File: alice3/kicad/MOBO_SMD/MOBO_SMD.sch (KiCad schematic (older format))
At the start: 0 parts

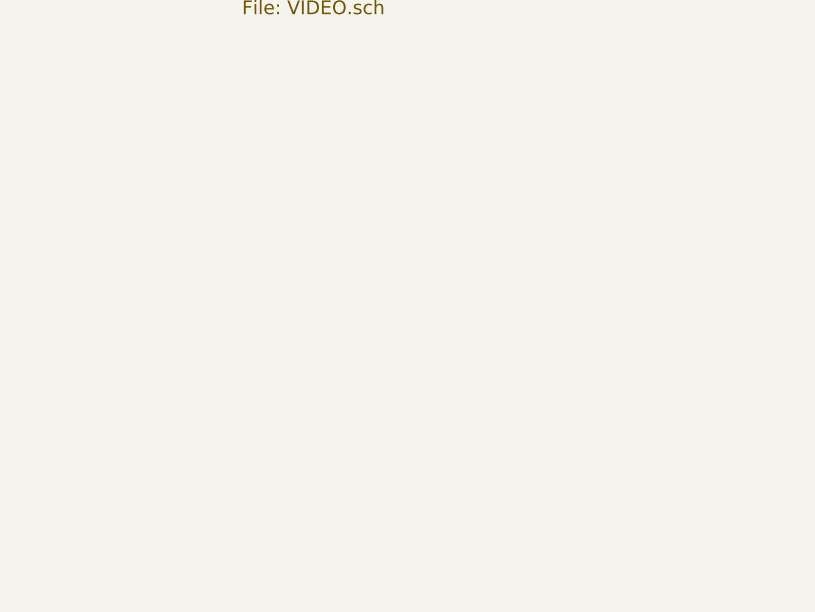
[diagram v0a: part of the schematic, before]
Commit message: Continuing to integrate STM32F415RG parts
Power circuit
STM32F415RG power and ground and BOOT pins
MicroSD card component and footprint
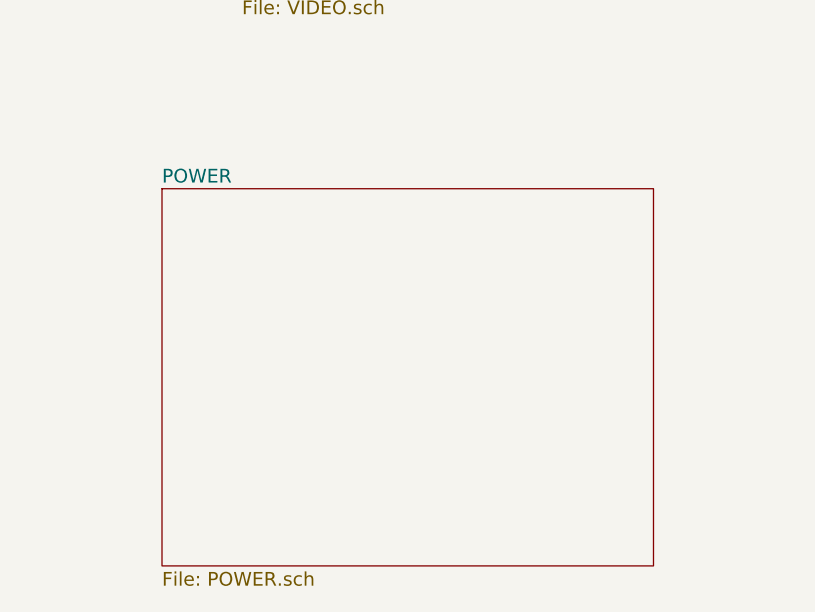
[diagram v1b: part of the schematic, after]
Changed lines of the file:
@@
 LIBS:conn
 LIBS:linear
-LIBS:regul
 LIBS:74xx
 LIBS:cmos4000
@@
 LIBS:km681000blp-7
 LIBS:stm32f415rg
+LIBS:regul
+LIBS:ldo
 LIBS:MOBO_SMD-cache
 EELAYER 25 0
@@
 $Descr A4 11693 8268
 encoding utf-8
-Sheet 1 4
+Sheet 1 5
 Title ""
 Date ""
@@
 F1 "CPU.sch" 60
 $EndSheet
+$Sheet
+S 4250 4100 2150 1650
+U 56BA9956
+F0 "POWER" 60
+F1 "POWER.sch" 60
+$EndSheet
 $EndSCHEMATC
